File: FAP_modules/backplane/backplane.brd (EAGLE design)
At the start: 160 x 100 mm, 45 parts, among them IC1 REG1117, J1 USB-MICROB, U1 STM32F10XRXT6

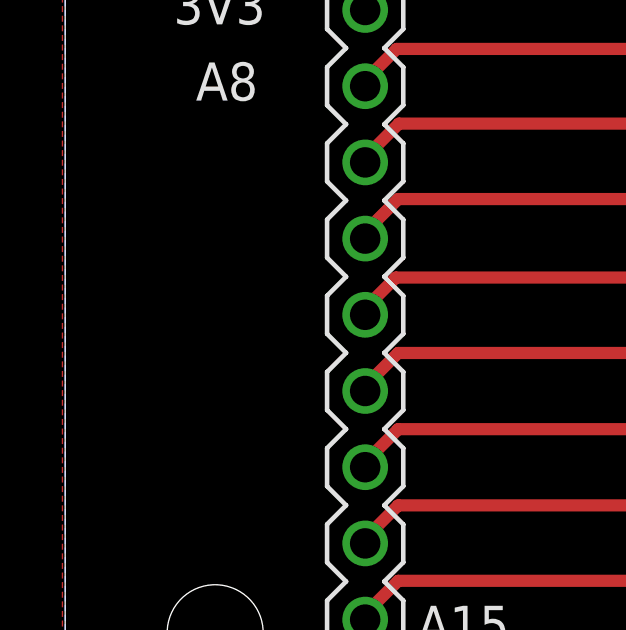
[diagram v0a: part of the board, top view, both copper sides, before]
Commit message: added GND test headers
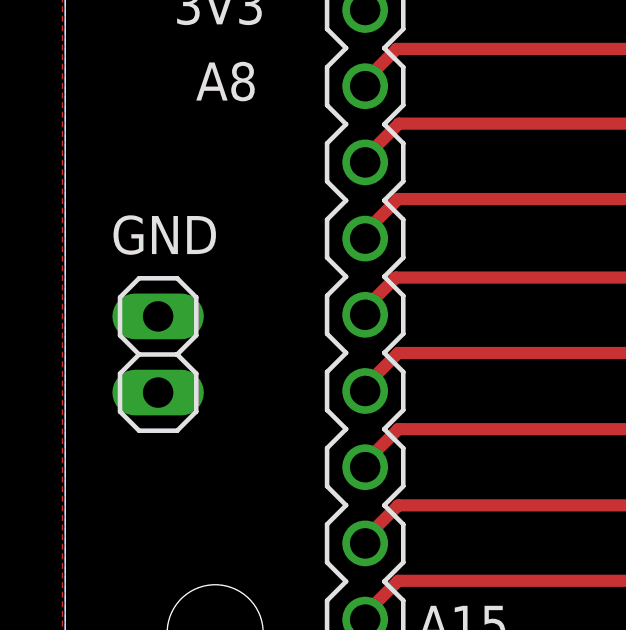
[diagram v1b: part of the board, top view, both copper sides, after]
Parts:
- added JP5: (no value), pinhead:1X02
- R2: value 10K -> 1K5
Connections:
- net GND: now also JP5.1, JP5.2
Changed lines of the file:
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@@
 <?xml version="1.0" encoding="utf-8"?>
 <!DOCTYPE eagle SYSTEM "eagle.dtd">
-<eagle version="7.6.0">
+<eagle version="7.7.0">
 <drawing>
 <settings>
@@
 <text x="142.4686" y="7.493" size="0.8128" layer="25">PA9</text>
 <text x="116.586" y="54.864" size="1.016" layer="25" rot="R90">5V</text>
+<text x="1.524" y="17.6222" size="1.27" layer="25">GND</text>
 </plain>
 <attributes>
@@
 <attribute name="NAME" x="154.8946" y="81.7753" size="0.4064" layer="25"/>
 </element>
-<element name="R2" library="SparkFun-Passives" package="0805" value="10K" x="137.5464" y="23.6474" smashed="yes" rot="R270">
+<element name="R2" library="SparkFun-Passives" package="0805" value="1K5" x="137.5464" y="23.6474" smashed="yes" rot="R270">
 <attribute name="NAME" x="138.7021" y="24.384" size="0.8128" layer="25" rot="R270"/>
 </element>
@@
 <element name="U$13" library="m3_mounting_hole" package="M3_MOUNTING_HOLE_PACK" value="M3_MOUNTING_HOLE" x="107" y="97"/>
 <element name="U$14" library="m3_mounting_hole" package="M3_MOUNTING_HOLE_PACK" value="M3_MOUNTING_HOLE" x="122" y="24"/>
+<element name="JP5" library="pinhead" package="1X02" value="" x="3.0988" y="14.2748" smashed="yes" rot="R90">
+<attribute name="VALUE" x="6.2738" y="11.7348" size="1.27" layer="27" rot="R90"/>
+</element>
 </elements>
 <signals>
@@
 <wire x1="131.186" y1="42.724" x2="131.1872" y2="42.7228" width="0.3048" layer="1"/>
 <wire x1="131.1872" y1="42.7228" x2="132.2378" y2="42.7228" width="0.3048" layer="1"/>
+<contactref element="JP5" pad="1"/>
+<contactref element="JP5" pad="2"/>
 </signal>
 <signal name="+3V3">

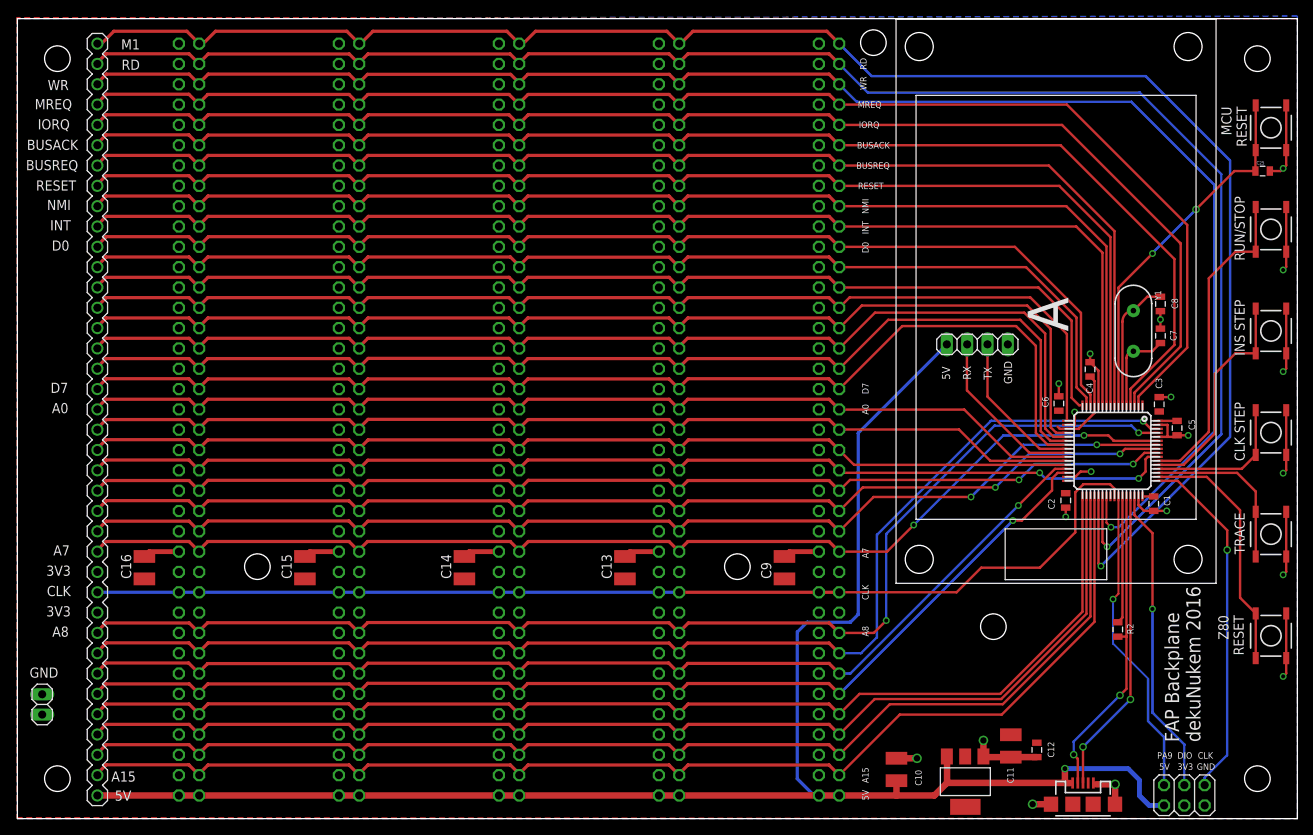
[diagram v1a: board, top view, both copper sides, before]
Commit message: added interrupt chaining and WAIT
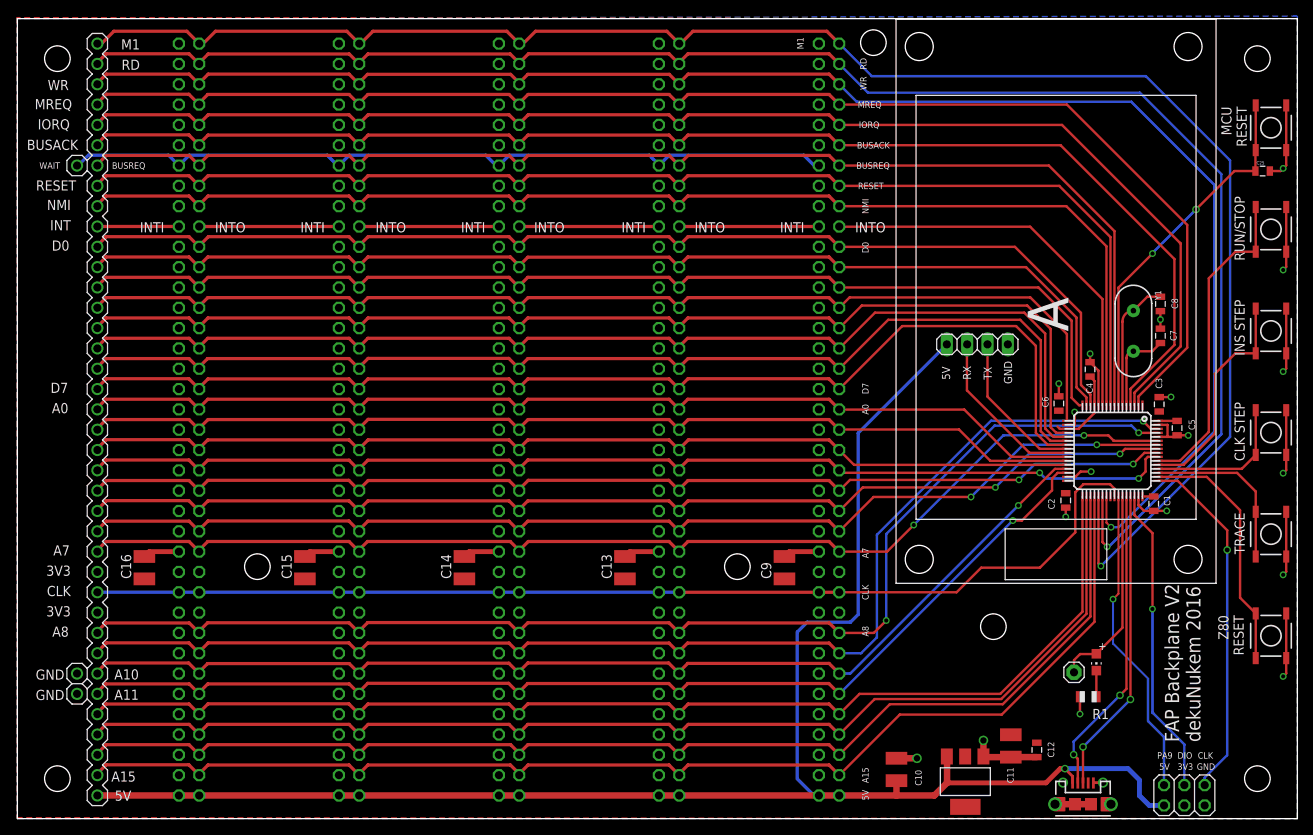
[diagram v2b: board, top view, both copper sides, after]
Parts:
- removed JP5: (no value), pinhead:1X02
- removed R2: 1K5, SparkFun-Passives:0805
- added JP2: (no value), adafruit:1X01
- added LED1: (no value), adafruit:CHIP-LED0805
- added R1: (no value), adafruit:R0805
- J1: device SparkFun-Connectors:USB-MICROB -> v3:USB-MICROB
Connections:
- removed net N$19: JP3.29, U$1.INT, U$2.INT, U$4.INT, U$5.INT, U$6.INT, U1.11
- new net N$1: JP3.29, U$6.INTI
- new net N$10: U$2.INTI, U$5.INTO
- new net N$12: LED1.C, R1.2
- new net N$15: JP3.WAIT, U$1.WAIT, U$2.WAIT, U$4.WAIT, U$5.WAIT, U$6.WAIT
- new net N$2: U$5.INTI, U$6.INTO
- new net N$5: U$1.INTO, U$4.INTI
- new net N$6: U$1.INTI, U$2.INTO
- new net N$8: U$4.INTO, U1.11
- net GND: now also J1.P1, J1.P2, J1.P3, J1.P4, J1.P5, J1.P6, JP3.GND1, JP3.GND2, R1.1; no longer J1.MT1, J1.MT2, JP5.1, JP5.2, U$1.GND@29, U$1.GND@32, U$2.GND@29, U$2.GND@32, U$4.GND@29, U$4.GND@32, U$5.GND@29, U$5.GND@32, U$6.GND@29, U$6.GND@32
- net N$61: now also JP2.1, LED1.A; no longer R2.1
- net N$96: no longer R2.2
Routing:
- net N$19: track 151.8 -> 0.00 mm
- net N$15: track 0.00 -> 98.2 mm
- net N$8: track 0.00 -> 49.9 mm
- net N$6: track 0.00 -> 17.5 mm
- net N$10: track 0.00 -> 17.5 mm
- net N$2: track 0.00 -> 17.5 mm
- net N$5: track 0.00 -> 17.5 mm
- net N$1: track 0.00 -> 10.2 mm
- net N$61: track 16.0 -> 25.7 mm
- net N$12: track 0.00 -> 3.27 mm
- net N$96: track 39.9 -> 38.8 mm
- net GND: track 122.3 -> 122.6 mm, vias 19 -> 18
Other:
- board text added: "A10"
- board text added: "A11"
- board text added: "FAP Backplane V2 dekuNukem 2016"
- board text added: "INTI"
- board text added: "INTO"
- board text added: "WAIT"
- board text removed: "FAP Backplane dekuNukem 2016"

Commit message: board cleanup
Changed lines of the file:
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@@
 <text x="116.586" y="54.864" size="1.016" layer="25" rot="R90">5V</text>
 <text x="2.286" y="17.3682" size="1.27" layer="25">GND</text>
-<text x="18.3642" y="74.5544" size="1.27" layer="25" rot="R180">INTI</text>
-<text x="28.5242" y="74.5544" size="1.27" layer="25" rot="R180">INTO</text>
-<text x="38.4302" y="74.5544" size="1.27" layer="25" rot="R180">INTI</text>
-<text x="48.5902" y="74.5544" size="1.27" layer="25" rot="R180">INTO</text>
-<text x="58.4962" y="74.5544" size="1.27" layer="25" rot="R180">INTI</text>
-<text x="68.4022" y="74.5544" size="1.27" layer="25" rot="R180">INTO</text>
-<text x="78.5622" y="74.5544" size="1.27" layer="25" rot="R180">INTI</text>
-<text x="88.4682" y="74.5544" size="1.27" layer="25" rot="R180">INTO</text>
-<text x="98.3742" y="74.5544" size="1.27" layer="25" rot="R180">INTI</text>
-<text x="108.5342" y="74.5544" size="1.27" layer="25" rot="R180">INTO</text>
+<text x="17.8562" y="74.5544" size="1.27" layer="25" rot="R180">INTI</text>
+<text x="29.0322" y="74.5544" size="1.27" layer="25" rot="R180">INTO</text>
+<text x="37.9222" y="74.5544" size="1.27" layer="25" rot="R180">INTI</text>
+<text x="49.0982" y="74.5544" size="1.27" layer="25" rot="R180">INTO</text>
+<text x="57.7342" y="74.5544" size="1.27" layer="25" rot="R180">INTI</text>
+<text x="69.1642" y="74.5544" size="1.27" layer="25" rot="R180">INTO</text>
+<text x="77.8002" y="74.5544" size="1.27" layer="25" rot="R180">INTI</text>
+<text x="89.2302" y="74.5544" size="1.27" layer="25" rot="R180">INTO</text>
+<text x="97.8662" y="74.5544" size="1.27" layer="25" rot="R180">INTI</text>
+<text x="109.0422" y="74.5544" size="1.27" layer="25" rot="R180">INTO</text>
 <text x="5.334" y="82.042" size="0.8128" layer="25" rot="R180">WAIT</text>
 <text x="2.286" y="14.8282" size="1.27" layer="25">GND</text>
@@
 <text x="12.1158" y="14.8536" size="1.27" layer="25">A11</text>
 <text x="98.278" y="96.1644" size="0.8128" layer="25" rot="R90">M1</text>
+<text x="98.044" y="82.042" size="0.8128" layer="25" rot="R180">WAIT</text>
 </plain>
 <attributes>

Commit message: added all Z80 signals on bus
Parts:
- removed JP2: (no value), adafruit:1X01
- moved LED1 9.49 mm to (138.8, 10.9), turned to 90 degrees
- moved R1 8.88 mm to (138.8, 7.87), turned to 180 degrees
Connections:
- removed net N$15: JP3.WAIT, U$1.WAIT, U$2.WAIT, U$4.WAIT, U$5.WAIT, U$6.WAIT
- removed net N$61: JP2.1, LED1.A, U1.43
- new net N$19: JP3.REFRESH, U$1.REFRESH, U$2.REFRESH, U$4.REFRESH, U$5.REFRESH, U$6.REFRESH
- new net N$21: JP3.HALT, U$1.HALT, U$2.HALT, U$4.HALT, U$5.HALT, U$6.HALT, U1.40
- new net N$27: JP3.WAIT, U$1.WAIT, U$2.WAIT, U$4.WAIT, U$5.WAIT, U$6.WAIT, U1.43
- net +3V3: now also LED1.A
- net GND: no longer R1.1, U$1.GND@31, U$1.GND@33, U$2.GND@31, U$2.GND@33, U$4.GND@31, U$4.GND@33, U$5.GND@31, U$5.GND@33, U$6.GND@31, U$6.GND@33
- net N$67: now also R1.1
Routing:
- net N$21: track 0.00 -> 198.1 mm, vias 0 -> 1
- net N$27: track 0.00 -> 179.9 mm, vias 0 -> 1
- net N$19: track 0.00 -> 98.3 mm
- net N$15: track 98.2 -> 0.00 mm
- net N$61: track 25.7 -> 0.00 mm
- net N$67: track 39.0 -> 44.1 mm
- net GND: track 122.6 -> 120.4 mm, vias 18 -> 17
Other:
- board text added: "HALT"
- board text added: "REFRESH"

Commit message: board cleanup
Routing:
- net GND: track 120.4 -> 129.8 mm
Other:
- board text added: "1"
- board text added: "2"
- board text added: "3"
- board text added: "4"
- board text added: "75"
- board text added: "76"
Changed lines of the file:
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@@
 <text x="98.044" y="84.582" size="0.8128" layer="25" rot="R180">HALT</text>
 <text x="98.298" y="79.375" size="0.8128" layer="25" rot="R180">REFRESH</text>
+<text x="38.6842" y="97.6684" size="1.27" layer="25" rot="R180">1</text>
+<text x="45.2882" y="97.6684" size="1.27" layer="25" rot="R180">2</text>
+<text x="38.6842" y="95.1284" size="1.27" layer="25" rot="R180">3</text>
+<text x="45.2882" y="95.1284" size="1.27" layer="25" rot="R180">4</text>
+<text x="38.1762" y="3.6884" size="1.27" layer="25" rot="R180">75</text>
+<text x="46.5582" y="3.6884" size="1.27" layer="25" rot="R180">76</text>
+<text x="78.3082" y="97.6684" size="1.27" layer="25" rot="R180">1</text>
+<text x="85.4202" y="97.6684" size="1.27" layer="25" rot="R180">2</text>
+<text x="78.3082" y="95.1284" size="1.27" layer="25" rot="R180">3</text>
+<text x="85.4202" y="95.1284" size="1.27" layer="25" rot="R180">4</text>
+<text x="78.3082" y="3.4344" size="1.27" layer="25" rot="R180">75</text>
+<text x="86.1822" y="3.4344" size="1.27" layer="25" rot="R180">76</text>
 </plain>
 <attributes>
@@
 <wire x1="129.703" y1="1.8034" x2="132.203" y2="1.8034" width="0.8128" layer="1"/>
 <wire x1="132.203" y1="1.8034" x2="134.203" y2="1.8034" width="0.8128" layer="1"/>
-<wire x1="131.186" y1="42.724" x2="131.044" y2="38.8764" width="0" layer="19" extent="1-1"/>
+<wire x1="134.219" y1="43.3832" x2="133.5078" y2="44.0944" width="0.2032" layer="16"/>
+<wire x1="133.5078" y1="44.0944" x2="127.6858" y2="44.0944" width="0.2032" layer="16"/>
+<wire x1="127.6858" y1="44.0944" x2="126.5682" y2="42.9768" width="0.2032" layer="16"/>
+<wire x1="126.5682" y1="42.9768" x2="126.5682" y2="42.0116" width="0.2032" layer="16"/>
 </signal>
 <signal name="+3V3">
@@
 <wire x1="11.0998" y1="44.831" x2="10" y2="43.7312" width="0.4064" layer="1"/>
 <wire x1="10" y1="43.7312" x2="10" y2="43.5380625" width="0.4064" layer="1"/>
-<via x="127.7874" y="43.2308" extent="1-16" drill="0.508"/>
-<wire x1="127.7874" y1="43.2308" x2="103.0348" y2="43.2308" width="0.3048" layer="1"/>
-<wire x1="103.0348" y1="43.2308" x2="102.73" y2="43.5356" width="0.3048" layer="1"/>
+<via x="128.0414" y="43.3578" extent="1-16" drill="0.508"/>
 <wire x1="142.586" y1="45.224" x2="141.617" y2="45.224" width="0.254" layer="1"/>
 <wire x1="141.617" y1="45.224" x2="140.9192" y2="44.5262" width="0.254" layer="1"/>
@@
 <wire x1="140.4112" y1="43.2816" x2="135.8392" y2="43.2816" width="0.254" layer="16"/>
 <wire x1="135.8392" y1="43.2816" x2="135.001" y2="42.4434" width="0.254" layer="16"/>
-<wire x1="135.001" y1="42.4434" x2="128.5748" y2="42.4434" width="0.254" layer="16"/>
-<wire x1="128.5748" y1="42.4434" x2="127.7874" y2="43.2308" width="0.254" layer="16"/>
+<wire x1="135.001" y1="42.4434" x2="128.9558" y2="42.4434" width="0.254" layer="16"/>
+<wire x1="128.9558" y1="42.4434" x2="128.0414" y2="43.3578" width="0.254" layer="16"/>
+<wire x1="128.0414" y1="43.3578" x2="102.9078" y2="43.3578" width="0.3048" layer="1"/>
+<wire x1="102.9078" y1="43.3578" x2="102.73" y2="43.5356" width="0.3048" layer="1"/>
 </signal>
 <signal name="N$48">
 <contactref element="U1" pad="56"/>
-<via x="139.4768" y="44.323" extent="1-16" drill="0.508"/>
-<wire x1="139.4768" y1="44.323" x2="140.8778" y2="45.724" width="0.3048" layer="1"/>
-<wire x1="140.8778" y1="45.724" x2="142.586" y2="45.724" width="0.3048" layer="1"/>
+<via x="139.4768" y="44.577" extent="1-16" drill="0.508"/>
 <contactref element="U$4" pad="A4"/>
 <contactref element="U$1" pad="A4"/>
@@
 <wire x1="11.1252" y1="42.2656" x2="10" y2="41.1404" width="0.4064" layer="1"/>
 <wire x1="10" y1="41.1404" x2="10" y2="40.9980625" width="0.4064" layer="1"/>
-<wire x1="139.4768" y1="44.323" x2="127.1778" y2="44.323" width="0.3048" layer="16"/>
-<wire x1="127.1778" y1="44.323" x2="125.1966" y2="42.3418" width="0.3048" layer="16"/>
 <via x="125.1966" y="42.3418" extent="1-16" drill="0.508"/>
 <wire x1="125.1966" y1="42.3418" x2="104.0762" y2="42.3418" width="0.3048" layer="1"/>
 <wire x1="104.0762" y1="42.3418" x2="102.73" y2="40.9956" width="0.3048" layer="1"/>
+<wire x1="142.586" y1="45.724" x2="140.6238" y2="45.724" width="0.254" layer="1"/>
+<wire x1="140.6238" y1="45.724" x2="139.4768" y2="44.577" width="0.254" layer="1"/>
+<wire x1="139.4768" y1="44.577" x2="127.4318" y2="44.577" width="0.254" layer="16"/>
+<wire x1="127.4318" y1="44.577" x2="125.1966" y2="42.3418" width="0.254" layer="16"/>
 </signal>
 <signal name="N$34">

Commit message: board cleanup
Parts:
- removed C11: 100uF, adafruit:C1210
- removed C12: 100nF, SparkFun-Capacitors:0805
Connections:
- net +3V3: no longer C11.1, C12.1
- net GND: no longer C11.2, C12.2
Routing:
- net GND: track 129.8 -> 123.2 mm
- net +3V3: track 14.2 -> 16.0 mm
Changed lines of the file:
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@@
 <attribute name="NAME" x="113.0354" y="4.1148" size="0.8128" layer="25" rot="R90"/>
-</element>
-<element name="C11" library="adafruit" package="C1210" value="100uF" x="124.1806" y="9.0878" smashed="yes" rot="R270">
-<attribute name="NAME" x="123.718" y="6.4008" size="0.8128" layer="25" rot="R270"/>
 </element>
 <element name="JP1" library="pinhead" package="1X04" value="" x="119.995" y="59.2836" smashed="yes" rot="R180">
@@
 <element name="C25" library="SparkFun-Capacitors" package="0805" value="100nF" x="155.6566" y="80.9498" smashed="yes">
 <attribute name="NAME" x="154.8946" y="81.7753" size="0.4064" layer="25"/>
-</element>
-<element name="C12" library="SparkFun-Capacitors" package="0805" value="100nF" x="127.4318" y="8.5906" smashed="yes" rot="R270">
-<attribute name="NAME" x="129.6035" y="7.64" size="0.8128" layer="25" rot="R90"/>
 </element>
 <element name="U$4" library="fap_bus_backplane" package="2X38" value="FAP_BUS" x="104" y="42.2656" smashed="yes" rot="R90"/>
@@
 <contactref element="C7" pad="2"/>
 <via x="130.1804" y="54.3814" extent="1-16" drill="0.508"/>
-<contactref element="C11" pad="2"/>
 <contactref element="C10" pad="2"/>
 <contactref element="JP1" pad="1"/>
@@
 <via x="143.672165625" y="38.47226875" extent="1-16" drill="0.508"/>
 <wire x1="140.136" y1="40.274" x2="140.136" y2="39.168" width="0.3048" layer="1"/>
-<contactref element="C12" pad="2"/>
 <contactref element="U$4" pad="GND@6"/>
 <contactref element="U$4" pad="GND@9"/>
@@
 <wire x1="95.885" y1="32.769" x2="96.4916" y2="33.3756" width="0.6096" layer="1"/>
 <wire x1="96.4916" y1="33.3756" x2="100.19" y2="33.3756" width="0.6096" layer="1"/>
-<wire x1="127.4318" y1="7.6906" x2="124.1834" y2="7.6906" width="0.8128" layer="1"/>
-<wire x1="124.1834" y1="7.6906" x2="124.1806" y2="7.6878" width="0.8128" layer="1"/>
-<wire x1="124.1806" y1="7.6878" x2="120.8416" y2="7.6878" width="0.8128" layer="1"/>
 <wire x1="120.8416" y1="7.6878" x2="120.757" y2="7.7724" width="0.8128" layer="1"/>
 <wire x1="140.136" y1="39.168" x2="140.834" y2="38.47" width="0.3048" layer="1"/>
@@
 <contactref element="C6" pad="1"/>
 <contactref element="IC1" pad="2"/>
-<contactref element="C11" pad="1"/>
-<wire x1="131.186" y1="48.724" x2="130.3006" y2="48.724" width="0.3048" layer="1"/>
-<wire x1="130.3006" y1="48.724" x2="130.0026" y2="49.022" width="0.3048" layer="1"/>
 <wire x1="134.636" y1="51.674" x2="134.636" y2="50.709" width="0.3048" layer="1"/>
 <wire x1="134.636" y1="50.709" x2="132.6442" y2="48.7172" width="0.3048" layer="1"/>
-<contactref element="C12" pad="1"/>
 <contactref element="JP4" pad="3"/>
 <wire x1="134.0812" y1="55.2594" x2="134.636" y2="54.7046" width="0.3048" layer="1"/>
@@
 <wire x1="132.6374" y1="48.724" x2="132.6442" y2="48.7172" width="0.3048" layer="1"/>
 <contactref element="LED1" pad="A"/>
+<wire x1="131.186" y1="48.724" x2="130.3714" y2="48.724" width="0.254" layer="1"/>
+<wire x1="130.3714" y1="48.724" x2="130.175" y2="48.9204" width="0.254" layer="1"/>
+<wire x1="130.175" y1="48.9204" x2="130.175" y2="50.9868" width="0.254" layer="1"/>
+<wire x1="130.175" y1="50.9868" x2="130.1804" y2="50.9922" width="0.254" layer="1"/>
 </signal>
 <signal name="N$14">
@@
 <contactref element="U1" pad="59"/>
 <via x="133.33" y="47.9044" extent="1-16" drill="0.508"/>
-<wire x1="142.586" y1="47.224" x2="137.033" y2="47.224" width="0.3048" layer="1"/>
 <wire x1="136.378" y1="47.9044" x2="133.33" y2="47.9044" width="0.3048" layer="1"/>
 <wire x1="133.33" y1="47.9044" x2="123.2408" y2="47.9044" width="0.3048" layer="16"/>
@@
 <wire x1="112.0394" y1="36.703" x2="108.712" y2="33.3756" width="0.3048" layer="1"/>
 <wire x1="108.712" y1="33.3756" x2="102.73" y2="33.3756" width="0.3048" layer="1"/>
-<wire x1="137.033" y1="47.224" x2="137.033" y2="47.2494" width="0.3048" layer="1"/>
-<wire x1="137.033" y1="47.2494" x2="136.378" y2="47.9044" width="0.3048" layer="1"/>
+<wire x1="142.586" y1="47.224" x2="137.0584" y2="47.224" width="0.3048" layer="1"/>
+<wire x1="137.0584" y1="47.224" x2="136.378" y2="47.9044" width="0.3048" layer="1"/>
 </signal>
 <signal name="N$31">

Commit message: board cleanup
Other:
- board text added: "FAP80 Backplane V2 dekuNukem 2016"
- board text removed: "FAP Backplane V2 dekuNukem 2016"
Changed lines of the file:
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@@
 <setting verticaltext="up"/>
 </settings>
-<grid distance="1" unitdist="mil" unit="mil" style="lines" multiple="1" display="no" altdistance="0.000123031496" altunitdist="mil" altunit="mil"/>
+<grid distance="10" unitdist="mil" unit="mil" style="lines" multiple="1" display="no" altdistance="0.000123031496" altunitdist="mil" altunit="mil"/>
 <layers>
 <layer number="1" name="Top" color="4" fill="1" visible="yes" active="yes"/>
@@
 <text x="106.152" y="93.6244" size="0.8128" layer="25" rot="R90">RD</text>
 <text x="106.406" y="75.5904" size="0.8128" layer="25" rot="R90">NMI</text>
-<text x="147.8842" y="9.5758" size="1.778" layer="25" rot="R90">FAP Backplane V2
+<text x="147.8842" y="9.3218" size="1.651" layer="25" rot="R90">FAP80 Backplane V2
 dekuNukem 2016</text>
 <text x="14.8082" y="5.8982" size="1.27" layer="25" rot="R180">A15</text>
